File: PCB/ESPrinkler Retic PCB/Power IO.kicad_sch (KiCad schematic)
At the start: 23 parts, among them J1 Conn_01x02, J5 Conn_01x02, J6 Conn_01x02, J7 Conn_01x10, Q2 Q_NMOS, Q3 Q_NMOS, U2 LM2596S-5

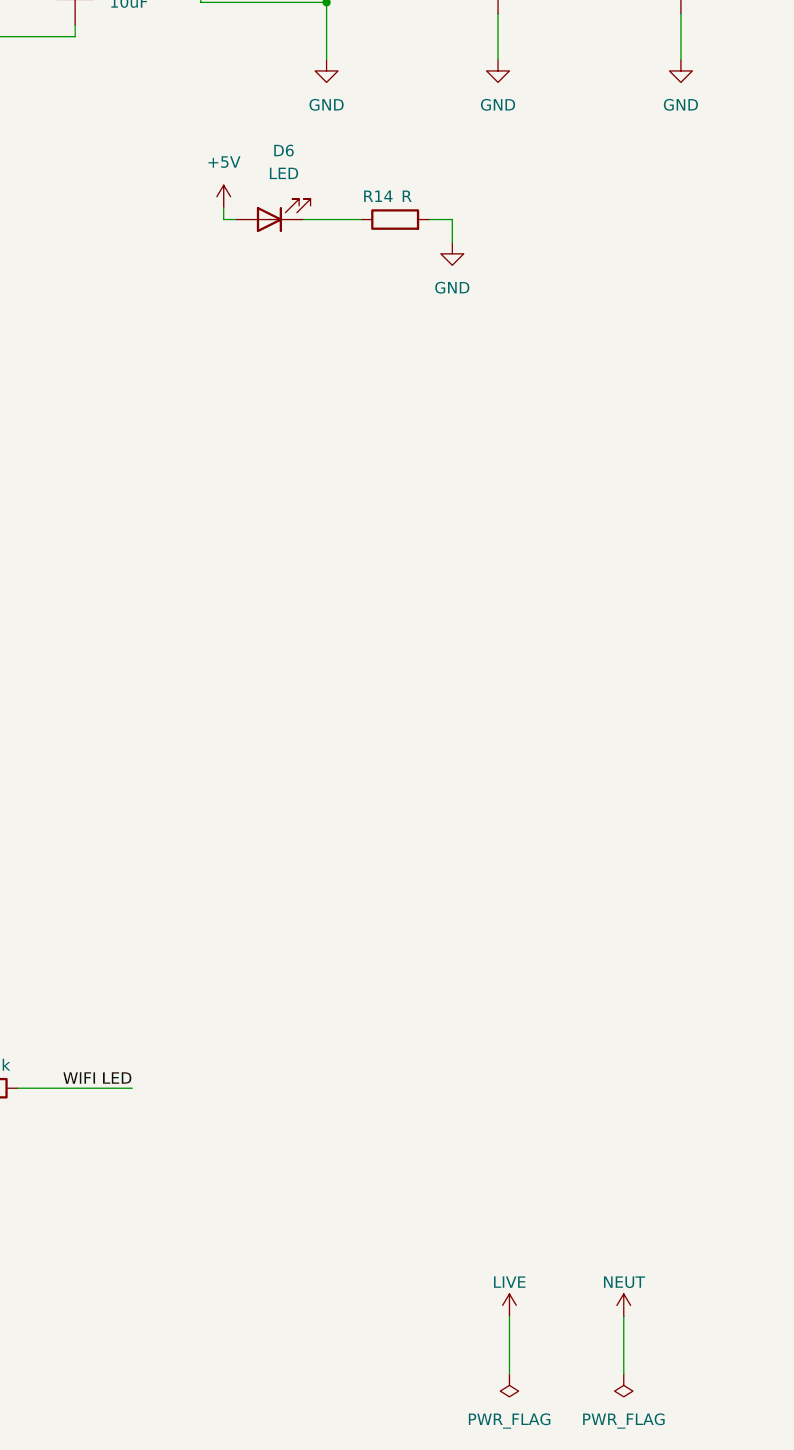
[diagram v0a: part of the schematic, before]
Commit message: Lay out control schematic and begin choosing parts
Source parts for existing symbols on the control schematic after laying out pump and zone circuits
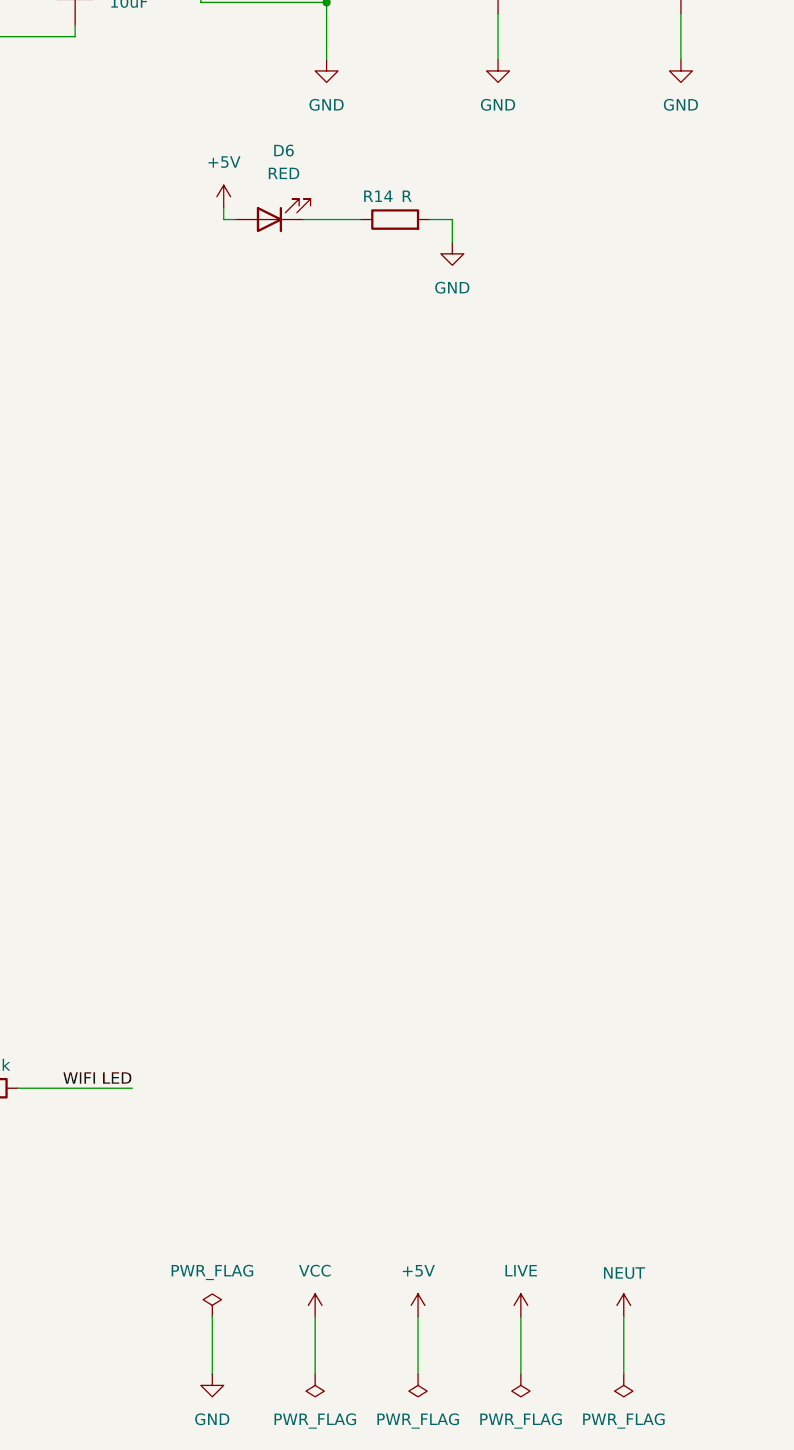
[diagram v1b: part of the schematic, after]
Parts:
- D6: value LED -> RED; footprint (none) -> LED_SMD:LED_0603_1608Metric; Manufacturer (none) -> Hubei KENTO Elec; Manufacturer P/N (none) -> KT-0603R; Supplier (none) -> LCSC; Supplier P/N (none) -> C2286

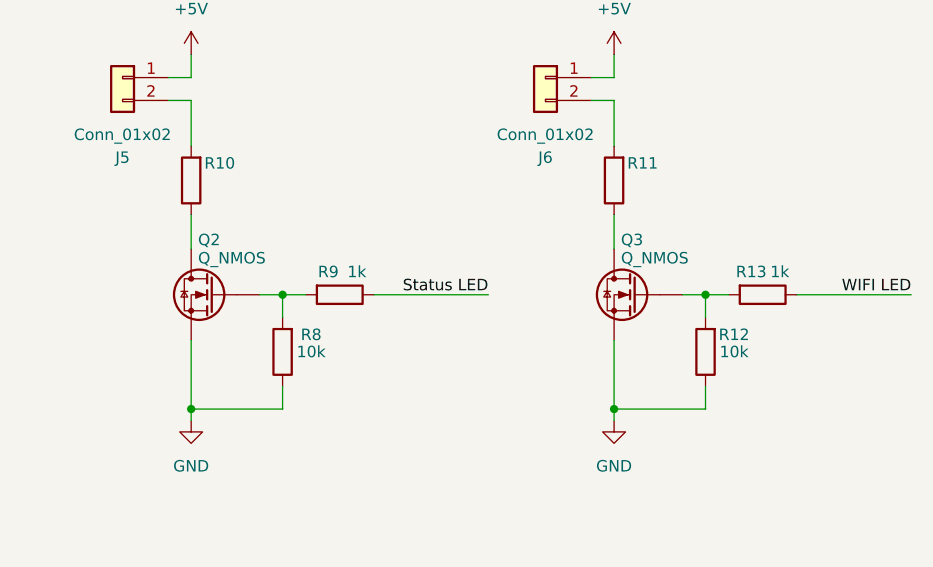
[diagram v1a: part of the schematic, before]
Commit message: Continue parts sourcing for existing components
Continue to source parts from LCSC for the existing components.
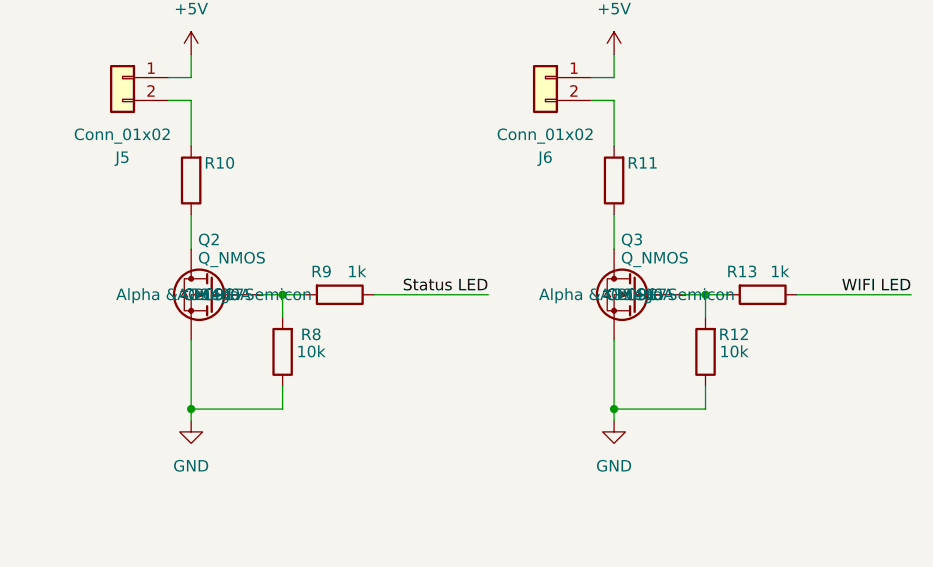
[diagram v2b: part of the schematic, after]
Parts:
- Q2, Q3: footprint (none) -> Package_TO_SOT_SMD:SOT-23_Handsoldering; Manufacturer (none) -> Alpha & Omega Semicon; Manufacturer P/N (none) -> AO3400A; Supplier (none) -> LCSC; Supplier P/N (none) -> C20917
- R12, R8: footprint (none) -> Resistor_SMD:R_0805_2012Metric; Manufacturer (none) -> UNI-ROYAL(Uniroyal Elec); Manufacturer P/N (none) -> 0805W8F1002T5E; Supplier (none) -> LCSC; Supplier P/N (none) -> C17414
- R13, R9: footprint (none) -> Resistor_SMD:R_0805_2012Metric; Manufacturer (none) -> UNI-ROYAL(Uniroyal Elec); Manufacturer P/N (none) -> 0805W8F1001T5E; Supplier (none) -> LCSC; Supplier P/N (none) -> C17513
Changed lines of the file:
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@@
 			)
 		)
-		(property "Datasheet" "~"
+		(property "Datasheet" ""
 			(at 132.08 60.96 0)
 			(effects
@@
 		(dnp no)
 		(property "Reference" "R9"
-			(at 52.07 154.94 90)
+			(at 51.308 154.94 90)
 			(effects
 				(font
@@
 			)
 		)
-		(property "Footprint" ""
+		(property "Footprint" "Resistor_SMD:R_0805_2012Metric"
 			(at 53.34 155.702 90)
 			(effects
@@
 			)
 		)
-		(property "Datasheet" "~"
+		(property "Datasheet" ""
 			(at 53.34 157.48 0)
 			(effects
@@
 			)
 		)
-		(property "Manufacturer" ""
+		(property "Manufacturer" "UNI-ROYAL(Uniroyal Elec)"
 			(at 53.34 157.48 0)
 			(effects
@@
 			)
 		)
-		(property "Manufacturer P/N" ""
+		(property "Manufacturer P/N" "0805W8F1001T5E"
 			(at 53.34 157.48 0)
 			(effects
@@
 			)
 		)
-		(property "Supplier" ""
+		(property "Supplier" "LCSC"
 			(at 53.34 157.48 0)
 			(effects
@@
 			)
 		)
-		(property "Supplier P/N" ""
+		(property "Supplier P/N" "C17513"
 			(at 53.34 157.48 0)
 			(effects
@@
 			)
 		)
-		(property "Datasheet" "~"
+		(property "Datasheet" ""
 			(at 146.05 60.96 0)
 			(effects
@@
 			)
 		)
-		(property "Footprint" ""
+		(property "Footprint" "Resistor_SMD:R_0805_2012Metric"
 			(at 95.758 163.83 90)
 			(effects
@@
 			)
 		)
-		(property "Datasheet" "~"
+		(property "Datasheet" ""
 			(at 93.98 163.83 0)
 			(effects
@@
 			)
 		)
-		(property "Manufacturer" ""
+		(property "Manufacturer" "UNI-ROYAL(Uniroyal Elec)"
 			(at 93.98 163.83 0)
 			(effects
@@
 			)
 		)
-		(property "Manufacturer P/N" ""
+		(property "Manufacturer P/N" "0805W8F1002T5E"
 			(at 93.98 163.83 0)
 			(effects
@@
 			)
 		)
-		(property "Supplier" ""
+		(property "Supplier" "LCSC"
 			(at 93.98 163.83 0)
 			(effects
@@
 			)
 		)
-		(property "Supplier P/N" ""
+		(property "Supplier P/N" "C17414"
 			(at 93.98 163.83 0)
 			(effects
@@
 			)
 		)
-		(property "Footprint" ""
+		(property "Footprint" "Package_TO_SOT_SMD:SOT-23_Handsoldering"
 			(at 34.29 154.94 0)
 			(effects
@@
 			)
 		)
-		(property "Datasheet" "~"
+		(property "Datasheet" ""
 			(at 39.37 157.48 0)
 			(effects
@@
 				)
 				(hide yes)
+			)
+		)
+		(property "Manufacturer" "Alpha & Omega Semicon"
+			(at 39.37 157.48 0)
+			(effects
+				(font
+					(size 1.27 1.27)
+				)
+			)
+		)
+		(property "Manufacturer P/N" "AO3400A"
+			(at 39.37 157.48 0)
+			(effects
+				(font
+					(size 1.27 1.27)
+				)
+			)
+		)
+		(property "Supplier" "LCSC"
+			(at 39.37 157.48 0)
+			(effects
+				(font
+					(size 1.27 1.27)
+				)
+			)
+		)
+		(property "Supplier P/N" "C20917"
+			(at 39.37 157.48 0)
+			(effects
+				(font
+					(size 1.27 1.27)
+				)
 			)
 		)
@@
 			)
 		)
-		(property "Footprint" ""
+		(property "Footprint" "Package_TO_SOT_SMD:SOT-23_Handsoldering"
 			(at 81.28 154.94 0)
 			(effects
@@
 			)
 		)
-		(property "Datasheet" "~"
+		(property "Datasheet" ""
 			(at 86.36 157.48 0)
 			(effects
@@
 				)
 				(hide yes)
+			)
+		)
+		(property "Manufacturer" "Alpha & Omega Semicon"
+			(at 86.36 157.48 0)
+			(effects
+				(font
+					(size 1.27 1.27)
+				)
+			)
+		)
+		(property "Manufacturer P/N" "AO3400A"
+			(at 86.36 157.48 0)
+			(effects
+				(font
+					(size 1.27 1.27)
+				)
+			)
+		)
+		(property "Supplier" "LCSC"
+			(at 86.36 157.48 0)
+			(effects
+				(font
+					(size 1.27 1.27)
+				)
+			)
+		)
+		(property "Supplier P/N" "C20917"
+			(at 86.36 157.48 0)
+			(effects
+				(font
+					(size 1.27 1.27)
+				)
 			)
 		)
@@
 			)
 		)
-		(property "Datasheet" "~"
+		(property "Datasheet" ""
 			(at 25.4 86.36 0)
 			(effects
@@
 		(dnp no)
 		(property "Reference" "R13"
-			(at 99.06 154.94 90)
+			(at 98.044 154.94 90)
 			(effects
 				(font
@@
 			)
 		)
-		(property "Footprint" ""
+		(property "Footprint" "Resistor_SMD:R_0805_2012Metric"
 			(at 100.33 155.702 90)
 			(effects
@@
 			)
 		)
-		(property "Datasheet" "~"
+		(property "Datasheet" ""
 			(at 100.33 157.48 0)
 			(effects
@@
 			)
 		)
-		(property "Manufacturer" ""
+		(property "Manufacturer" "UNI-ROYAL(Uniroyal Elec)"
 			(at 100.33 157.48 0)
 			(effects
@@
 			)
 		)
-		(property "Manufacturer P/N" ""
+		(property "Manufacturer P/N" "0805W8F1001T5E"
 			(at 100.33 157.48 0)
 			(effects
@@
 			)
 		)
-		(property "Supplier" ""
+		(property "Supplier" "LCSC"
 			(at 100.33 157.48 0)
 			(effects
@@
 			)
 		)
-		(property "Supplier P/N" ""
+		(property "Supplier P/N" "C17513"
 			(at 100.33 157.48 0)
 			(effects
@@
 			)
 		)
-		(property "Footprint" ""
+		(property "Footprint" "Resistor_SMD:R_0805_2012Metric"
 			(at 48.768 163.83 90)
 			(effects
@@
 			)
 		)
-		(property "Datasheet" "~"
+		(property "Datasheet" ""
 			(at 46.99 163.83 0)
 			(effects
@@
 			)
 		)
-		(property "Manufacturer" ""
+		(property "Manufacturer" "UNI-ROYAL(Uniroyal Elec)"
 			(at 46.99 163.83 0)
 			(effects
@@
 			)
 		)
-		(property "Manufacturer P/N" ""
+		(property "Manufacturer P/N" "0805W8F1002T5E"
 			(at 46.99 163.83 0)
 			(effects
@@
 			)
 		)
-		(property "Supplier" ""
+		(property "Supplier" "LCSC"
 			(at 46.99 163.83 0)
 			(effects
@@
 			)
 		)
-		(property "Supplier P/N" ""
+		(property "Supplier P/N" "C17414"
 			(at 46.99 163.83 0)
 			(effects
